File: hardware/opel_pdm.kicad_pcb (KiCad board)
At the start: 2 copper layers, 99.5 x 75 mm, 46 parts, among them P001 CANCONNECTOR, P002 CONN_01X14, P100 ISP, P101 DEBUG_LED, U401 MCP2551-I/SN, U403 LPC11C14, U501 MCP1755-33, U502 MCP1755-5, U6 TCA9543A, U7 LTC2943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

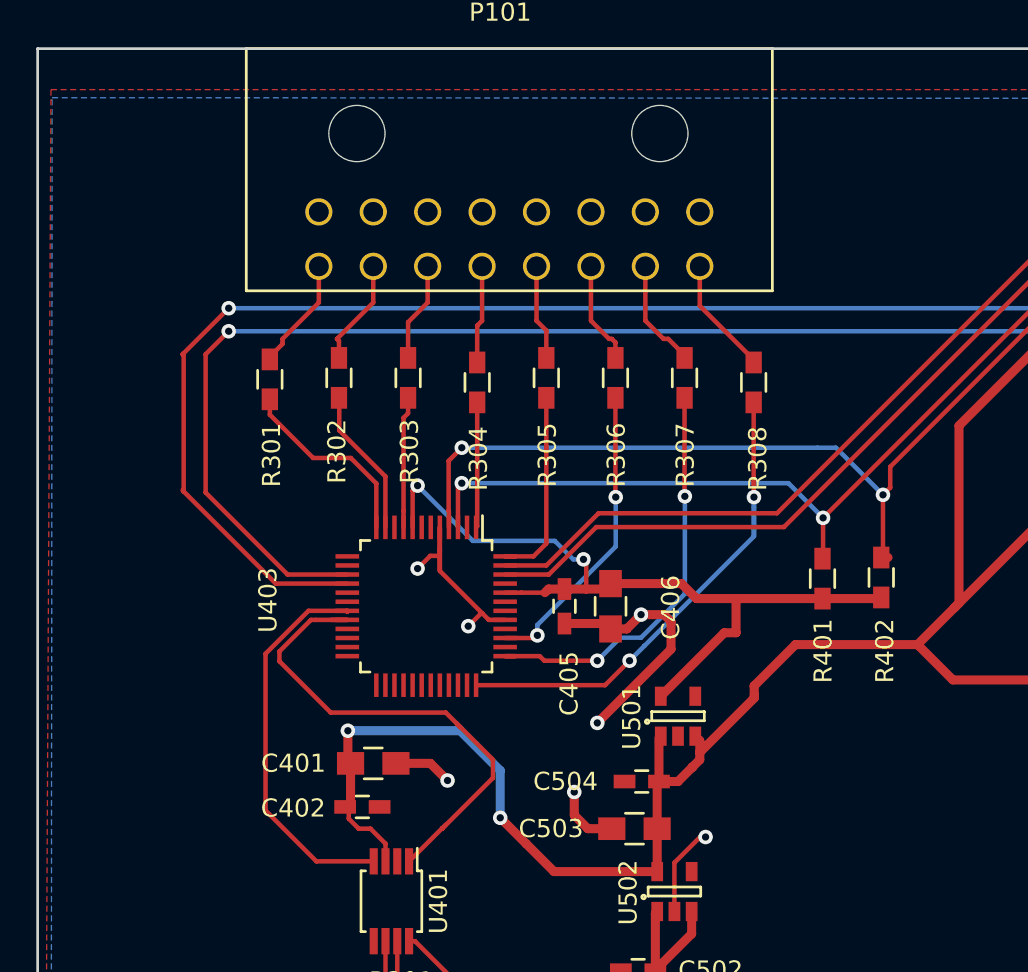
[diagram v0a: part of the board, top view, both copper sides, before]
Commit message: Added LEDs and another decoupling capacitor to board.
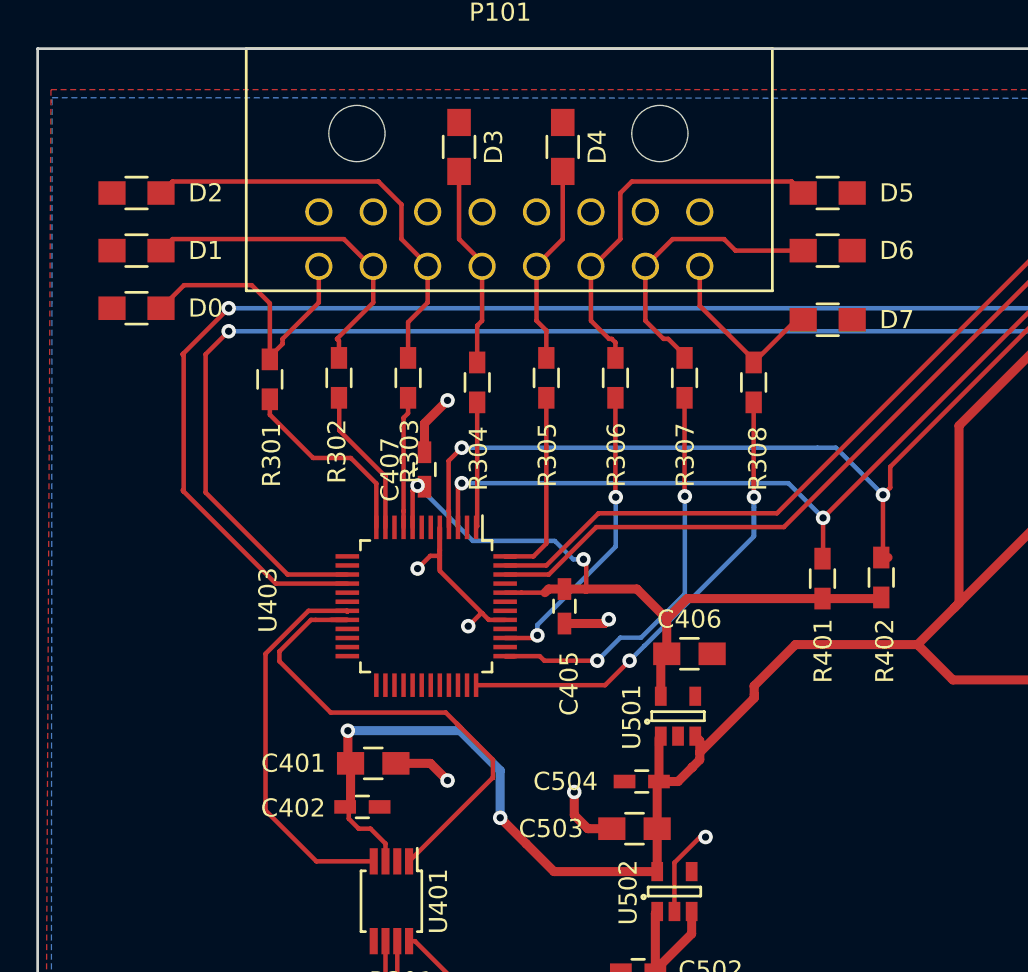
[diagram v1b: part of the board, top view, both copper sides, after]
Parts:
- added C407: 0.1uF, Capacitors_SMD:C_0603_HandSoldering, F.Cu at (123.8, 76.2)
- added D0: Led_Small, Resistors_SMD:R_0805_HandSoldering, F.Cu at (108.0, 67.3)
- added D1: Led_Small, Resistors_SMD:R_0805_HandSoldering, F.Cu at (108.0, 64.1)
- added D2: Led_Small, Resistors_SMD:R_0805_HandSoldering, F.Cu at (108.0, 61.0)
- added D3: Led_Small, Resistors_SMD:R_0805_HandSoldering, F.Cu at (125.7, 58.4)
- added D4: Led_Small, Resistors_SMD:R_0805_HandSoldering, F.Cu at (131.4, 58.4)
- added D5: Led_Small, Resistors_SMD:R_0805_HandSoldering, F.Cu at (146.1, 61.0)
- added D6: Led_Small, Resistors_SMD:R_0805_HandSoldering, F.Cu at (146.1, 64.1)
- added D7: Led_Small, Resistors_SMD:R_0805_HandSoldering, F.Cu at (146.1, 67.9)
- moved C406 5.08 mm to (138.4, 86.4), turned to 0 degrees
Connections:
- net +12V renamed /Power_Supplies/+12V
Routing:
- net Net-(D2-Pad2): track 5.50 -> 23.5 mm
- net Net-(D5-Pad2): track 5.70 -> 21.1 mm
- net Net-(D1-Pad2): track 5.92 -> 18.5 mm
- net Net-(D0-Pad2): track 6.25 -> 16.3 mm
- net Net-(D6-Pad2): track 6.10 -> 15.7 mm
- net GND: track 108.2 -> 100.4 mm
- net Net-(D4-Pad2): track 5.27 -> 11.1 mm
- net Net-(D3-Pad2): track 5.41 -> 11.2 mm
- net Net-(D7-Pad2): track 6.53 -> 10.2 mm
- net +3V3: track 43.8 -> 41.8 mm

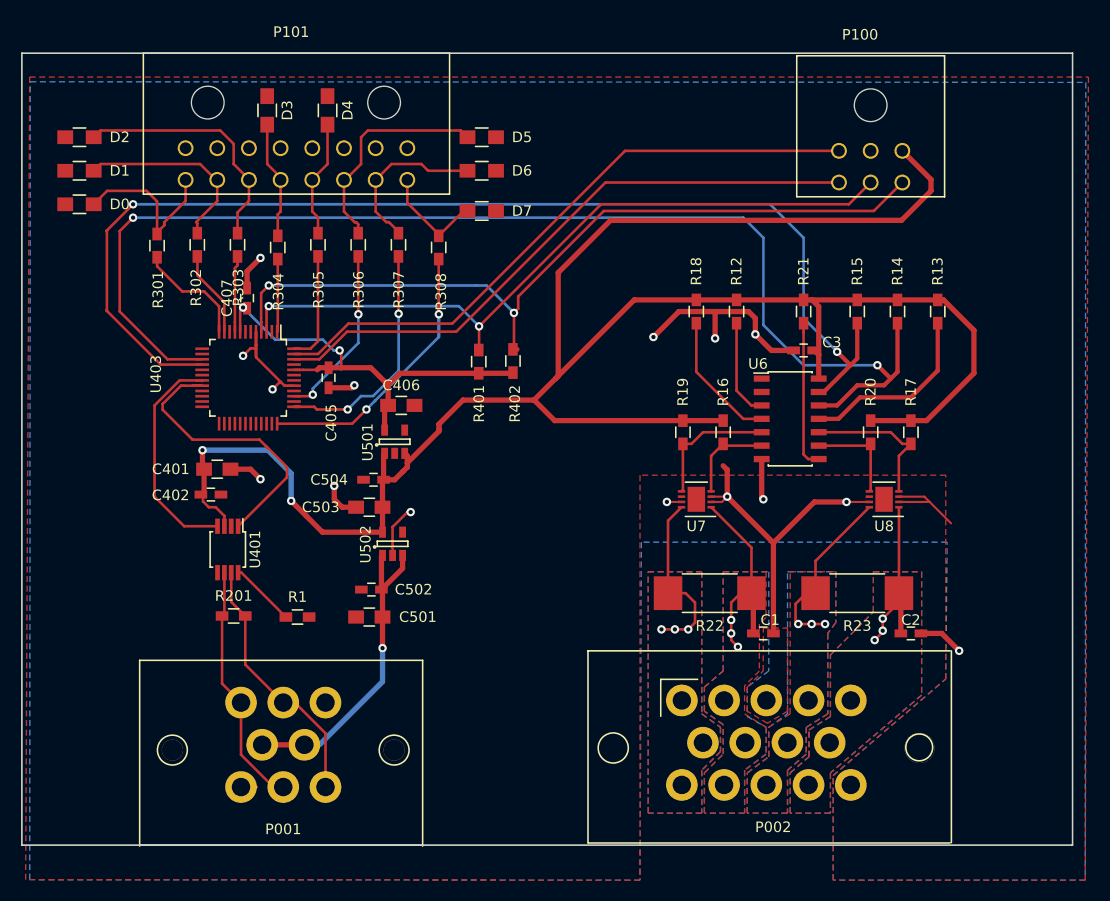
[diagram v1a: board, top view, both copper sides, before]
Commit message: Added test points, LEDs, 3D model to board.
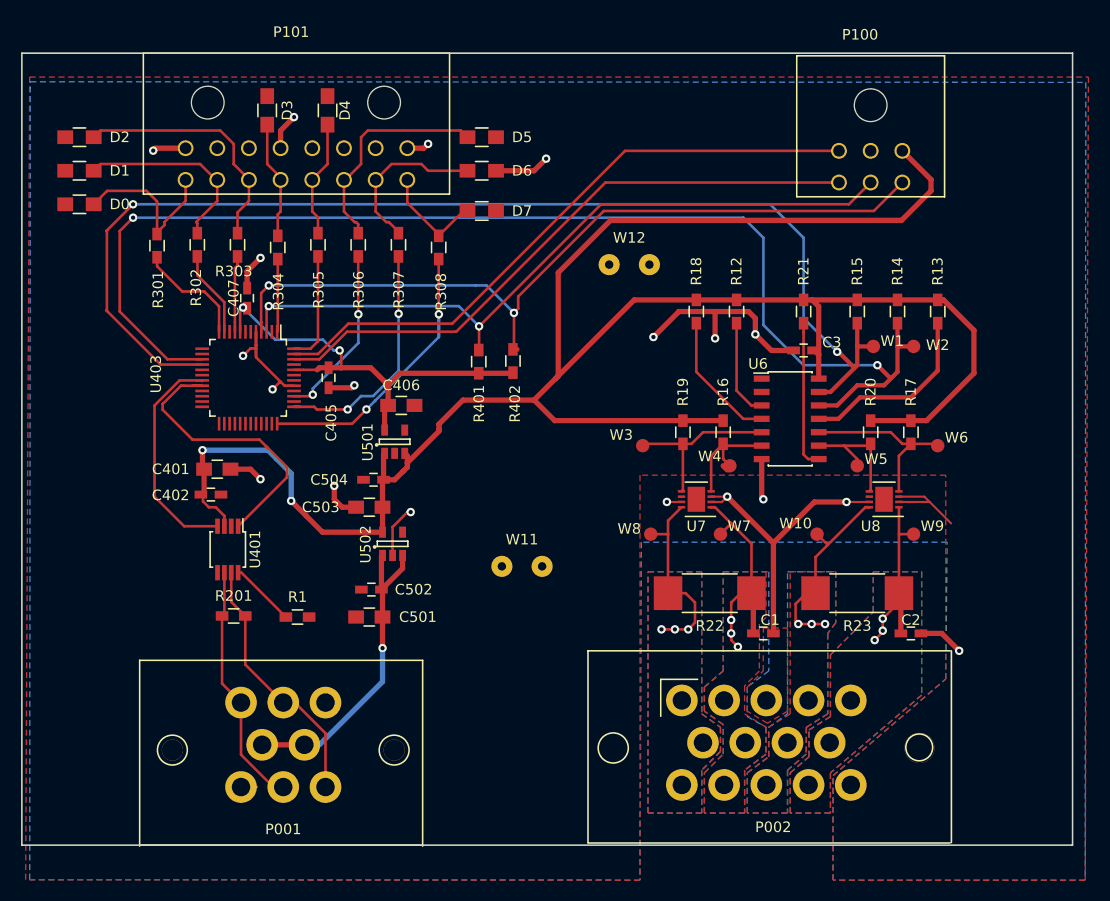
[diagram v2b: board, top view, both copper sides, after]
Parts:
- added W1: SDA, MITEVT_TP:smd_test_pad, F.Cu at (183.1, 80.8)
- added W10: LV-, MITEVT_TP:smd_test_pad, F.Cu at (177.8, 98.6)
- added W11: TST_GND, Wire_Pads:SolderWirePad_2x_0-8mmDrill, F.Cu at (149.9, 101.6)
- added W12: TST_GND, Wire_Pads:SolderWirePad_2x_0-8mmDrill, F.Cu at (160.0, 73.0)
- added W2: SCL, MITEVT_TP:smd_test_pad, F.Cu at (186.9, 80.8)
- added W3: SD0, MITEVT_TP:smd_test_pad, F.Cu at (161.3, 90.2)
- added W4: SC0, MITEVT_TP:smd_test_pad, F.Cu at (169.5, 92.1)
- added W5: SD1, MITEVT_TP:smd_test_pad, F.Cu at (181.6, 92.1)
- added W6: SD1, MITEVT_TP:smd_test_pad, F.Cu at (189.2, 90.2)
- added W7: CS+, MITEVT_TP:smd_test_pad, F.Cu at (168.7, 98.6)
- added W8: CS-, MITEVT_TP:smd_test_pad, F.Cu at (162.1, 98.6)
- added W9: LV+, MITEVT_TP:smd_test_pad, F.Cu at (186.9, 98.6)
- D0: value Led_Small -> PIO2_8
- D1: value Led_Small -> PIO2_7
- D2: value Led_Small -> PIO1_8
- D3: value Led_Small -> PIO2_6
- D4: value Led_Small -> PIO3_3
- D5: value Led_Small -> PIO1_3
- D6: value Led_Small -> PIO3_1
- D7: value Led_Small -> PIO3_0
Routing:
- net GND: track 100.4 -> 111.3 mm, vias 15 -> 19
- net Net-(R19-Pad2): track 12.5 -> 16.3 mm
- net /I2C Multiplexer and Gas Gauges/SDA: track 109.5 -> 112.5 mm
- net Net-(R16-Pad2): track 8.69 -> 11.6 mm
- net Net-(R17-Pad2): track 14.2 -> 16.8 mm
- net Net-(R20-Pad2): track 9.54 -> 12.0 mm
- net /BACK_PANEL/CS_SENSE+: track 21.6 -> 23.7 mm
- net /BACK_PANEL/LV_SENSE-: track 17.9 -> 19.8 mm
- net /BACK_PANEL/CS_SENSE-: track 20.0 -> 21.7 mm
- net /BACK_PANEL/LV_SENSE+: track 18.6 -> 20.2 mm
- net /I2C Multiplexer and Gas Gauges/SCL: track 115.4 -> 116.9 mm
